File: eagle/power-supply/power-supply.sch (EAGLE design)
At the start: 15 parts, among them IC1 7805, IC2 7905, J1 1751251, J2 1751251, Q1 MJL1302A, Q2 MJL3281A

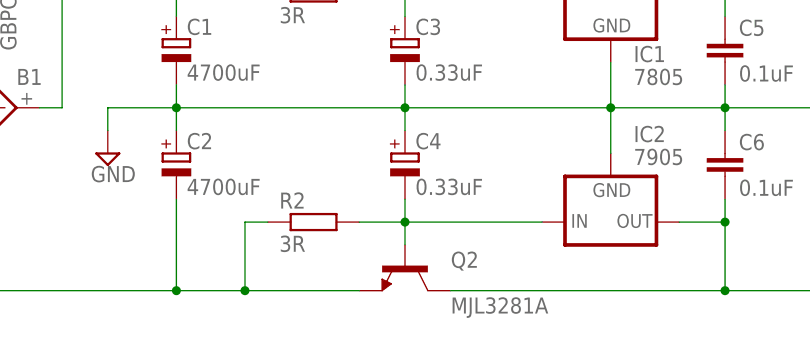
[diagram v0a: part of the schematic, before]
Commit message: Fixes to power supply circuit and board design
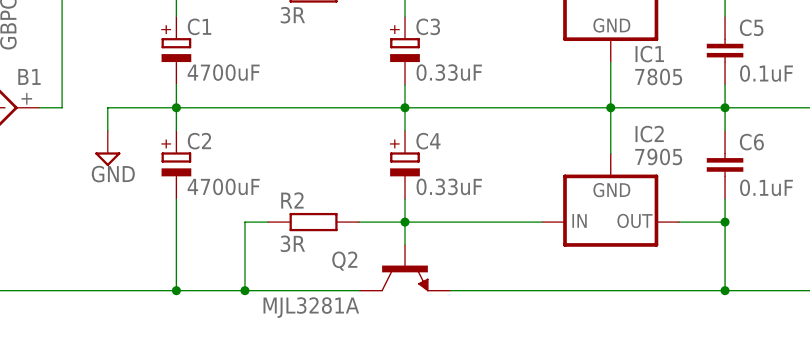
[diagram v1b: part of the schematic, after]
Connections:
- net N$11: now also Q2.EMITTER; no longer Q2.COLLECTOR
- net N$8: now also Q2.COLLECTOR; no longer Q2.EMITTER
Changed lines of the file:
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@@
 <part name="R1" library="resistor" deviceset="R-EU_" device="0411/15" value="3R"/>
 <part name="R2" library="resistor" deviceset="R-EU_" device="0411/15" value="3R"/>
-<part name="Q1" library="MJL1302A-MJL3281A" deviceset="MJL1302A" device=""/>
-<part name="Q2" library="MJL1302A-MJL3281A" deviceset="MJL3281A" device=""/>
+<part name="Q1" library="MJL1302A-MJL3281A" deviceset="MJL1302A" device="" value="MJL1302A"/>
+<part name="Q2" library="MJL1302A-MJL3281A" deviceset="MJL3281A" device="" value="MJL3281A"/>
 <part name="C3" library="rcl" deviceset="CPOL-EU" device="E2.5-5" value="0.33uF"/>
 <part name="C4" library="rcl" deviceset="CPOL-EU" device="E2.5-5" value="0.33uF"/>
@@
 <attribute name="VALUE" x="119.38" y="78.74" size="1.778" layer="96" rot="R180"/>
 </instance>
-<instance part="Q2" gate="G$1" x="101.6" y="43.18" smashed="yes" rot="R270">
-<attribute name="NAME" x="106.68" y="43.18" size="1.778" layer="95"/>
-<attribute name="VALUE" x="106.68" y="38.1" size="1.778" layer="96"/>
+<instance part="Q2" gate="G$1" x="101.6" y="43.18" smashed="yes" rot="MR270">
+<attribute name="NAME" x="96.52" y="43.18" size="1.778" layer="95" rot="MR0"/>
+<attribute name="VALUE" x="96.52" y="38.1" size="1.778" layer="96" rot="MR0"/>
 </instance>
 <instance part="C3" gate="G$1" x="101.6" y="68.58"/>
@@
 <pinref part="C6" gate="G$1" pin="2"/>
 <wire x1="137.16" y1="50.8" x2="137.16" y2="48.26" width="0.1524" layer="91"/>
-<junction x="137.16" y="40.64"/>
 <wire x1="137.16" y1="48.26" x2="137.16" y2="40.64" width="0.1524" layer="91"/>
 <wire x1="137.16" y1="40.64" x2="147.32" y2="40.64" width="0.1524" layer="91"/>
 <wire x1="147.32" y1="40.64" x2="147.32" y2="50.8" width="0.1524" layer="91"/>
 <wire x1="147.32" y1="50.8" x2="152.4" y2="50.8" width="0.1524" layer="91"/>
-<pinref part="Q2" gate="G$1" pin="COLLECTOR"/>
-<wire x1="106.68" y1="40.64" x2="137.16" y2="40.64" width="0.1524" layer="91"/>
 <pinref part="J2" gate="-3" pin="K"/>
 <pinref part="IC2" gate="1" pin="OUT"/>
 <wire x1="132.08" y1="48.26" x2="137.16" y2="48.26" width="0.1524" layer="91"/>
 <junction x="137.16" y="48.26"/>
+<pinref part="Q2" gate="G$1" pin="EMITTER"/>
+<wire x1="106.68" y1="40.64" x2="137.16" y2="40.64" width="0.1524" layer="91"/>
+<junction x="137.16" y="40.64"/>
 </segment>
 </net>
@@
 <net name="N$8" class="0">
 <segment>
-<pinref part="Q2" gate="G$1" pin="EMITTER"/>
-<wire x1="96.52" y1="40.64" x2="83.82" y2="40.64" width="0.1524" layer="91"/>
 <wire x1="83.82" y1="40.64" x2="83.82" y2="48.26" width="0.1524" layer="91"/>
 <pinref part="R2" gate="G$1" pin="1"/>
@@
 <wire x1="83.82" y1="40.64" x2="76.2" y2="40.64" width="0.1524" layer="91"/>
 <junction x="76.2" y="40.64"/>
+<pinref part="Q2" gate="G$1" pin="COLLECTOR"/>
+<wire x1="96.52" y1="40.64" x2="83.82" y2="40.64" width="0.1524" layer="91"/>
 <junction x="83.82" y="40.64"/>
 </segment>
